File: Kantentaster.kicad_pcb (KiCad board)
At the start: 2 copper layers, 18 parts, among them U1 LM324

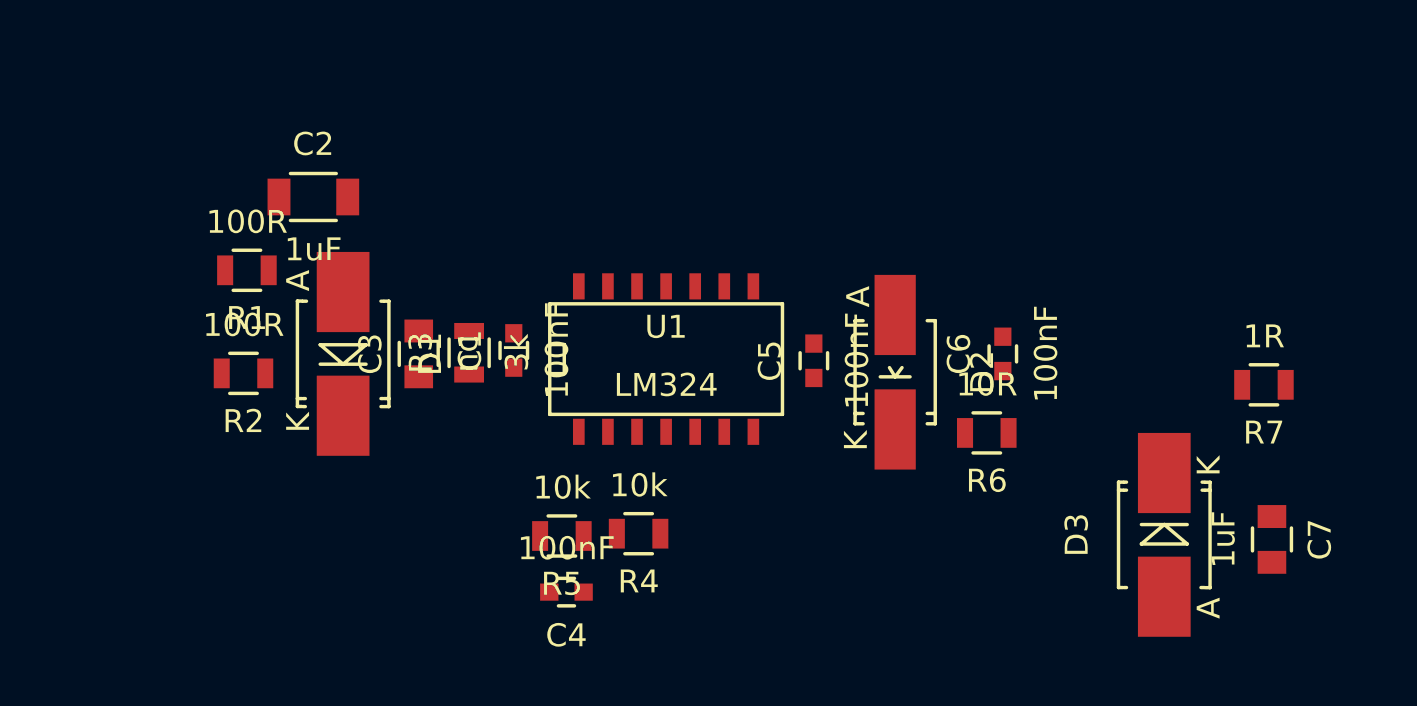
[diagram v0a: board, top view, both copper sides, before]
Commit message: anpassungen am schaltplan und layout
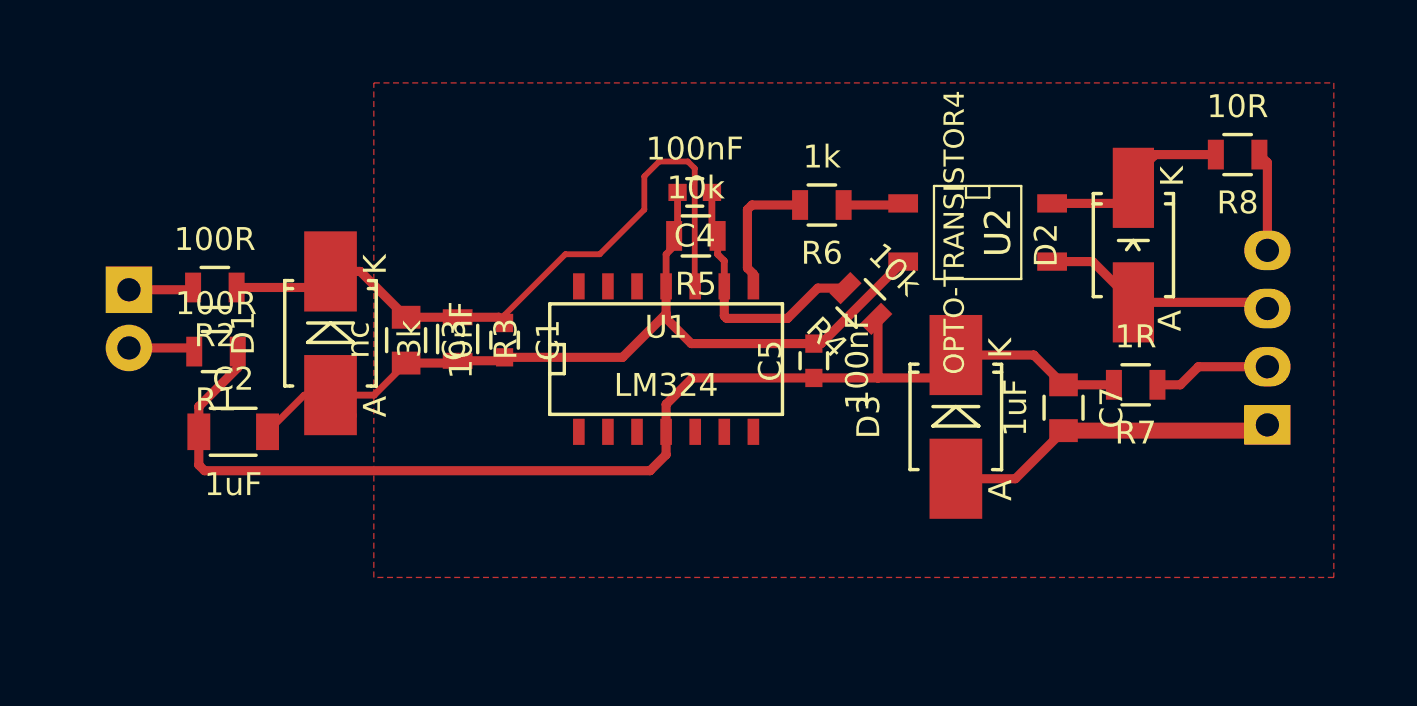
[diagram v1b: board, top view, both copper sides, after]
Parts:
- removed C6: 100nF, Capacitors_SMD:C_0603
- added P1: Anschluss Kantentaster, Pin_Headers:Pin_Header_Angled_1x02, B.Cu at (99.8, 99.2)
- added P2: CONN_01X04, Pin_Headers:Pin_Header_Angled_1x04, B.Cu at (149.5, 105.1)
- added R8: 10R, Resistors_SMD:R_0805, F.Cu at (148.2, 93.3)
- added U2: OPTO-TRANSISTOR4, toni:SO-4, F.Cu at (136.8, 96.7)
- C1: value 100nF -> 10nF
- D1: value ZENER_18V -> ZENER_15V
- D2: value ZENER_6,3V -> ZENER_15V
- R6: value 10R -> 1k
- moved C4 18.3 mm to (124.5, 95.0)
- moved R5 14.3 mm to (124.5, 96.8)
- moved R4 14.0 mm to (131.8, 99.8), turned to 135 degrees
- moved R6 12.3 mm to (130.1, 95.5)
- moved D2 11.8 mm to (143.7, 97.2), turned to 90 degrees
- moved C2 10.8 mm to (104.3, 105.4)
- moved C7 10.8 mm to (140.6, 104.3)
- moved D3 10.5 mm to (135.9, 104.8)
- moved R7 5.60 mm to (143.8, 103.3)
- moved R2 3.95 mm to (103.5, 99.1)
- moved R1 3.80 mm to (103.6, 101.9)
- moved D1 1.05 mm to (108.6, 101.1), turned to 90 degrees
- moved C3 0.81 mm to (111.9, 101.4), turned to 270 degrees
- moved R3 0.78 mm to (114.2, 101.3), turned to 270 degrees
- moved C1 0.60 mm to (116.2, 101.4), turned to 270 degrees
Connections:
- D2 pad 1: GND -> Net-(D2-Pad1)
- R6 pad 2: Net-(D2-Pad2) -> Net-(R6-Pad2)
- U1 pad 1: Net-(D2-Pad2) -> (no net)
- U1 pad 10: (no net) -> Net-(C1-Pad1)
- U1 pad 2: Net-(C4-Pad1) -> (no net)
- U1 pad 3: Net-(C1-Pad1) -> (no net)
- U1 pad 8: (no net) -> Net-(R6-Pad2)
- U1 pad 9: (no net) -> Net-(C4-Pad1)
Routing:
- net GND: track 0.00 -> 52.5 mm
- net +12V: track 0.00 -> 52.2 mm
- net Net-(C1-Pad1): track 0.00 -> 30.8 mm
- net Net-(C4-Pad1): track 0.00 -> 11.5 mm
- net Net-(D2-Pad1): track 0.00 -> 10.2 mm
- net Net-(D2-Pad2): track 0.00 -> 8.32 mm
- net Net-(R6-Pad2): track 0.00 -> 5.84 mm
- net Net-(P2-Pad2): track 0.00 -> 5.13 mm
- net Net-(P2-Pad4): track 0.00 -> 4.32 mm
- net Net-(P1-Pad2): track 0.00 -> 2.92 mm
- net Net-(P1-Pad1): track 0.00 -> 2.84 mm
- net Net-(R6-Pad1): track 0.00 -> 2.63 mm
- added copper zone on F.Cu, net GND
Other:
- net class 1 added: clearance 0.18, trace_width 0.254, via_dia 0.889, via_drill 0.635

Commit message: Mitkopplung hinzugefügt
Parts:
- added R9: 200k, Resistors_SMD:R_0805, F.Cu at (128.3, 93.3)
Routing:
- net Net-(C1-Pad1): track 30.8 -> 34.0 mm
- net Net-(R6-Pad2): track 5.84 -> 8.05 mm

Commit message: finale Version
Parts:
- added C6: 10nF, Capacitors_SMD:C_0603, F.Cu at (131.4, 95.9)
- moved R6 1.21 mm to (128.9, 95.9)
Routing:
- net GND: track 52.5 -> 228.9 mm
- net Net-(C6-Pad1): track 2.63 -> 4.28 mm
- net Net-(R6-Pad2): track 8.05 -> 6.60 mm

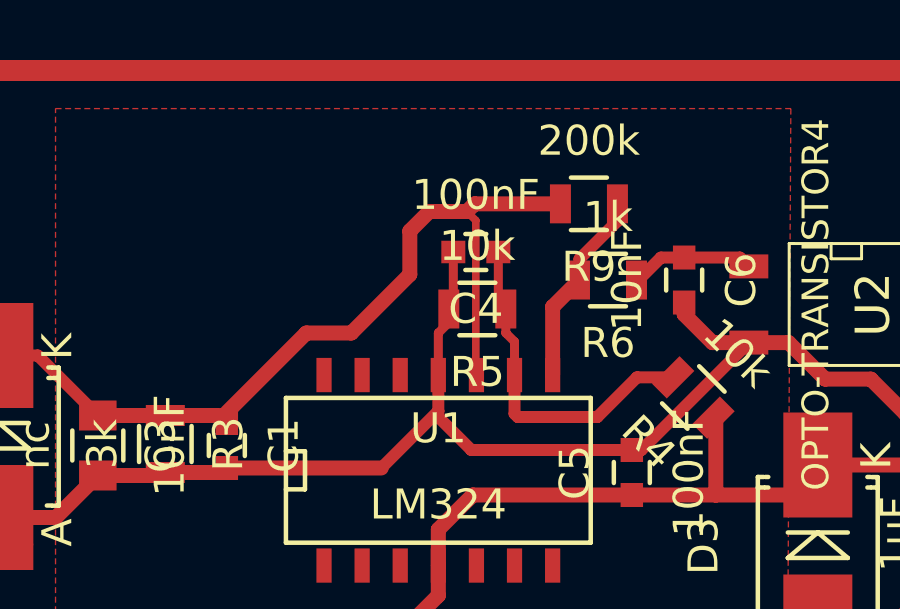
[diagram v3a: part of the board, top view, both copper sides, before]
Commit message: Fehler des ersten Prototypen behoben
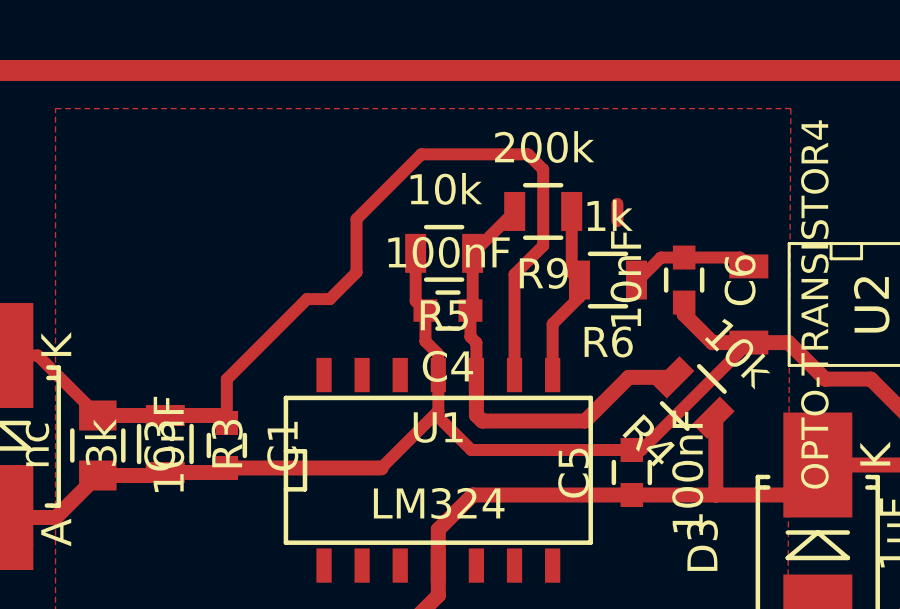
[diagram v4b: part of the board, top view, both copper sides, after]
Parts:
- moved C4 2.16 mm to (123.6, 96.9)
- moved R5 2.16 mm to (123.4, 95.0)
- moved R9 1.55 mm to (126.7, 93.6)
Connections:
- R9 pad 2: Net-(C1-Pad1) -> Net-(C4-Pad1)
- U1 pad 10: Net-(C1-Pad1) -> Net-(C4-Pad1)
- U1 pad 9: Net-(C4-Pad1) -> Net-(C1-Pad1)
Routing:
- net Net-(C4-Pad1): track 11.5 -> 14.8 mm
- net Net-(C1-Pad1): track 34.0 -> 36.8 mm
- net Net-(R6-Pad2): track 6.60 -> 5.93 mm
- net (no net): track 0.00 -> 0.57 mm
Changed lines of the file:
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@@
     (links 41)
     (no_connects 0)
-    (area 88.870999 88.55 160.429001 112.110001)
+    (area 0 0 0 0)
     (thickness 1.6)
     (drawings 0)
-    (tracks 131)
+    (tracks 134)
     (zones 0)
     (modules 23)
@@
   )
   (setup
-    (last_trace_width 0.7)
+    (last_trace_width 0.4)
     (user_trace_width 0.3)
     (user_trace_width 0.4)
@@
   )
   (module Capacitors_SMD:C_0603 (layer F.Cu)
-    (at 124.5 94.95 180)
+    (at 123.571 96.901 180)
     (descr "Capacitor SMD 0603, reflow soldering, AVX (see smccp.pdf)")
     (tags "capacitor 0603")
@@
   )
   (module Resistors_SMD:R_0805 (layer F.Cu)
-    (at 124.55 96.85 180)
+    (at 123.444 94.996 180)
     (descr "Resistor SMD 0805, reflow soldering, Vishay (see dcrcw.pdf)")
     (tags "resistor 0805")
@@
       (net 11 "Net-(R6-Pad2)"))
     (pad 9 smd rect (at 2.54 -3.048) (size 0.508 1.143) (layers F.Cu F.Paste F.Mask)
-      (net 4 "Net-(C4-Pad1)"))
+      (net 1 "Net-(C1-Pad1)"))
     (pad 11 smd rect (at 0 -3.048) (size 0.508 1.143) (layers F.Cu F.Paste F.Mask)
       (net 2 GND))
@@
     (pad 14 smd rect (at -3.81 -3.048) (size 0.508 1.143) (layers F.Cu F.Paste F.Mask))
     (pad 10 smd rect (at 1.27 -3.048) (size 0.508 1.143) (layers F.Cu F.Paste F.Mask)
-      (net 1 "Net-(C1-Pad1)"))
+      (net 4 "Net-(C4-Pad1)"))
     (model SMD_Packages/SOIC-14_N.wrl
       (at (xyz 0 0 0))
@@
   )
   (module Resistors_SMD:R_0805 (layer F.Cu)
-    (at 128.27 93.345 180)
+    (at 126.746 93.599 180)
     (descr "Resistor SMD 0805, reflow soldering, Vishay (see dcrcw.pdf)")
     (tags "resistor 0805")
@@
       (net 11 "Net-(R6-Pad2)"))
     (pad 2 smd rect (at 0.95 0 180) (size 0.7 1.3) (layers F.Cu F.Paste F.Mask)
-      (net 1 "Net-(C1-Pad1)"))
+      (net 4 "Net-(C4-Pad1)"))
     (model Resistors_SMD/R_0805.wrl
       (at (xyz 0 0 0))
@@
     )
   )
-  (segment (start 116.2 100.65) (end 116.2 100.3) (width 0.254) (layer F.Cu) (net 1))
-  (segment (start 116.2 100.3) (end 118.85 97.65) (width 0.5) (layer F.Cu) (net 1))
-  (segment (start 124.5 93.9) (end 124.5 99.032) (width 0.254) (layer F.Cu) (net 1))
-  (segment (start 124.2 93.6) (end 124.5 93.9) (width 0.254) (layer F.Cu) (net 1))
-  (segment (start 122.95 93.6) (end 124.2 93.6) (width 0.5) (layer F.Cu) (net 1))
-  (segment (start 122.3 94.25) (end 122.95 93.6) (width 0.5) (layer F.Cu) (net 1))
-  (segment (start 122.3 95.7) (end 122.3 94.25) (width 0.5) (layer F.Cu) (net 1))
-  (segment (start 120.35 97.65) (end 122.3 95.7) (width 0.5) (layer F.Cu) (net 1))
-  (segment (start 118.85 97.65) (end 120.35 97.65) (width 0.5) (layer F.Cu) (net 1))
-  (segment (start 124.5 99.032) (end 124.52 99.052) (width 0.254) (layer F.Cu) (net 1))
+  (segment (start 129.22 93.345) (end 129.22 93.919) (width 0.4) (layer F.Cu) (net 0))
+  (segment (start 116.2 100.65) (end 116.2 99.192) (width 0.4) (layer F.Cu) (net 1) (status 400000))
+  (segment (start 125.79 95.698) (end 125.79 99.052) (width 0.4) (layer F.Cu) (net 1) (status 800000))
+  (segment (start 126.746 94.742) (end 125.79 95.698) (width 0.4) (layer F.Cu) (net 1))
+  (segment (start 126.746 92.202) (end 126.746 94.742) (width 0.4) (layer F.Cu) (net 1))
+  (segment (start 126.238 91.694) (end 126.746 92.202) (width 0.4) (layer F.Cu) (net 1))
+  (segment (start 122.682 91.694) (end 126.238 91.694) (width 0.4) (layer F.Cu) (net 1))
+  (segment (start 120.523 93.853) (end 122.682 91.694) (width 0.4) (layer F.Cu) (net 1))
+  (segment (start 120.523 95.631) (end 120.523 93.853) (width 0.4) (layer F.Cu) (net 1))
+  (segment (start 119.634 96.52) (end 120.523 95.631) (width 0.4) (layer F.Cu) (net 1))
+  (segment (start 118.872 96.52) (end 119.634 96.52) (width 0.4) (layer F.Cu) (net 1))
+  (segment (start 116.2 99.192) (end 118.872 96.52) (width 0.4) (layer F.Cu) (net 1))
   (segment (start 114.15 100.4) (end 115.95 100.4) (width 0.5) (layer F.Cu) (net 1))
   (segment (start 115.95 100.4) (end 116.2 100.65) (width 0.4) (layer F.Cu) (net 1))
@@
   (segment (start 107.89998 99.1) (end 108.6 98.39998) (width 0.4) (layer F.Cu) (net 1))
   (segment (start 109.35 99.09998) (end 109.15 99.29998) (width 0.4) (layer F.Cu) (net 1))
-  (segment (start 124.205 93.6) (end 124.46 93.345) (width 0.5) (layer F.Cu) (net 1))
-  (segment (start 124.46 93.345) (end 127.32 93.345) (width 0.5) (layer F.Cu) (net 1))
-  (segment (start 124.2 93.6) (end 124.205 93.6) (width 0.3) (layer F.Cu) (net 1))
-  (segment (start 135.9 107.45002) (end 135.9 111.75) (width 0.7) (layer F.Cu) (net 2) (status 400000))
+  (segment (start 122.821 96.901) (end 122.809 96.901) (width 0.4) (layer F.Cu) (net 2))
+  (segment (start 122.809 96.901) (end 122.494 96.586) (width 0.4) (layer F.Cu) (net 2))
+  (segment (start 122.494 96.586) (end 122.494 94.996) (width 0.4) (layer F.Cu) (net 2))
+  (segment (start 123.25 99.052) (end 123.25 98.358) (width 0.4) (layer F.Cu) (net 2))
+  (segment (start 122.821 97.929) (end 122.821 96.901) (width 0.4) (layer F.Cu) (net 2))
+  (segment (start 123.25 98.358) (end 122.821 97.929) (width 0.4) (layer F.Cu) (net 2))
+  (segment (start 135.9 107.45002) (end 135.9 111.75) (width 0.7) (layer F.Cu) (net 2))
   (segment (start 99.06 111.76) (end 135.89 111.76) (width 0.7) (layer F.Cu) (net 2))
   (segment (start 96.52 109.22) (end 99.06 111.76) (width 0.7) (layer F.Cu) (net 2))
@@
   (segment (start 108.6 103.80002) (end 110.49998 103.80002) (width 0.5) (layer F.Cu) (net 2))
   (segment (start 110.49998 103.80002) (end 111.9 102.4) (width 0.5) (layer F.Cu) (net 2))
-  (segment (start 123.6 96.85) (end 123.6 97.3) (width 0.254) (layer F.Cu) (net 2))
-  (segment (start 123.6 97.3) (end 123.25 97.65) (width 0.3) (layer F.Cu) (net 2))
-  (segment (start 123.25 97.65) (end 123.25 99.052) (width 0.3) (layer F.Cu) (net 2))
-  (segment (start 123.75 94.95) (end 123.75 96.7) (width 0.3) (layer F.Cu) (net 2))
-  (segment (start 123.75 96.7) (end 123.6 96.85) (width 0.254) (layer F.Cu) (net 2))
   (segment (start 116.2 102.15) (end 121.35 102.15) (width 0.5) (layer F.Cu) (net 2))
   (segment (start 121.35 102.15) (end 123.25 100.25) (width 0.4) (layer F.Cu) (net 2))
@@
   (segment (start 139.29998 102.04998) (end 140.6 103.35) (width 0.5) (layer F.Cu) (net 3))
   (segment (start 140.6 103.35) (end 142.8 103.35) (width 0.5) (layer F.Cu) (net 3))
-  (segment (start 125.5 96.85) (end 125.5 97.65) (width 0.3) (layer F.Cu) (net 4))
-  (segment (start 125.79 97.94) (end 125.79 99.052) (width 0.3) (layer F.Cu) (net 4))
-  (segment (start 125.5 97.65) (end 125.79 97.94) (width 0.3) (layer F.Cu) (net 4))
-  (segment (start 125.25 94.95) (end 125.25 96.6) (width 0.3) (layer F.Cu) (net 4))
-  (segment (start 125.25 96.6) (end 125.5 96.85) (width 0.3) (layer F.Cu) (net 4))
-  (segment (start 125.79 99.052) (end 125.79 100.34) (width 0.4) (layer F.Cu) (net 4))
-  (segment (start 125.79 100.34) (end 125.9 100.45) (width 0.4) (layer F.Cu) (net 4))
-  (segment (start 125.9 100.45) (end 128.55 100.45) (width 0.4) (layer F.Cu) (net 4))
-  (segment (start 128.55 100.45) (end 129.871751 99.128249) (width 0.4) (layer F.Cu) (net 4))
-  (segment (start 129.871751 99.128249) (end 131.078249 99.128249) (width 0.4) (layer F.Cu) (net 4))
+  (segment (start 124.394 94.996) (end 124.399 94.996) (width 0.4) (layer F.Cu) (net 4) (status C00000))
+  (segment (start 124.399 94.996) (end 125.796 93.599) (width 0.4) (layer F.Cu) (net 4) (status C00000))
+  (segment (start 124.321 96.901) (end 124.321 97.778) (width 0.4) (layer F.Cu) (net 4))
+  (segment (start 124.52 97.977) (end 124.52 99.052) (width 0.4) (layer F.Cu) (net 4))
+  (segment (start 124.321 97.778) (end 124.52 97.977) (width 0.4) (layer F.Cu) (net 4))
+  (segment (start 124.394 94.996) (end 124.394 96.828) (width 0.4) (layer F.Cu) (net 4))
+  (segment (start 124.394 96.828) (end 124.321 96.901) (width 0.4) (layer F.Cu) (net 4))
+  (segment (start 124.52 99.052) (end 124.52 100.39) (width 0.5) (layer F.Cu) (net 4))
+  (segment (start 129.598751 99.128249) (end 131.078249 99.128249) (width 0.5) (layer F.Cu) (net 4))
+  (segment (start 128.143 100.584) (end 129.598751 99.128249) (width 0.5) (layer F.Cu) (net 4))
+  (segment (start 124.714 100.584) (end 128.143 100.584) (width 0.5) (layer F.Cu) (net 4))
+  (segment (start 124.52 100.39) (end 124.714 100.584) (width 0.5) (layer F.Cu) (net 4))
+  (segment (start 124.5 99.032) (end 124.52 99.052) (width 0.254) (layer F.Cu) (net 4))
   (segment (start 140.1012 95.43) (end 142.97064 95.43) (width 0.5) (layer F.Cu) (net 5))
   (segment (start 142.97064 95.43) (end 143.65 94.75064) (width 0.4) (layer F.Cu) (net 5))
@@
   (segment (start 149.5 97.48) (end 149.5 93.65) (width 0.5) (layer F.Cu) (net 10))
   (segment (start 149.5 93.65) (end 149.15 93.3) (width 0.5) (layer F.Cu) (net 10))
-  (segment (start 129.22 93.345) (end 129.22 93.919) (width 0.4) (layer F.Cu) (net 11))
-  (segment (start 129.22 93.919) (end 127.955 95.184) (width 0.4) (layer F.Cu) (net 11))
-  (segment (start 127.955 95.184) (end 127.955 95.885) (width 0.4) (layer F.Cu) (net 11))
-  (segment (start 127.06 99.052) (end 127.06 96.78) (width 0.5) (layer F.Cu) (net 11))
-  (segment (start 127.06 96.78) (end 127.955 95.885) (width 0.5) (layer F.Cu) (net 11))
+  (segment (start 127.06 99.052) (end 127.06 97.349) (width 0.4) (layer F.Cu) (net 11) (status 400000))
+  (segment (start 127.06 97.349) (end 127.955 96.454) (width 0.4) (layer F.Cu) (net 11) (status 800000))
+  (segment (start 127.955 96.454) (end 127.955 95.885) (width 0.4) (layer F.Cu) (net 11) (status C00000))
+  (segment (start 127.696 93.599) (end 127.696 95.626) (width 0.4) (layer F.Cu) (net 11) (status C00000))
+  (segment (start 127.696 95.626) (end 127.955 95.885) (width 0.4) (layer F.Cu) (net 11) (status C00000))
   (segment (start 131.445 95.135) (end 133.3038 95.135) (width 0.4) (layer F.Cu) (net 12))
   (segment (start 133.3038 95.135) (end 133.5988 95.43) (width 0.4) (layer F.Cu) (net 12))
